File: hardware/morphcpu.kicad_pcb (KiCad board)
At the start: 2 copper layers, 70 x 70 mm, 83 parts, among them J1 TYPE-C-31-M-12, SW1 RESET, U1 ICE40UP5K-SG48I, U2 FT231XS-R, U3 W25Q32JVSSIQ, U4 ME6211C33M5G-N, U5 ME6211C12M5G-N, X1 1532H4-16000JWPDTSNL

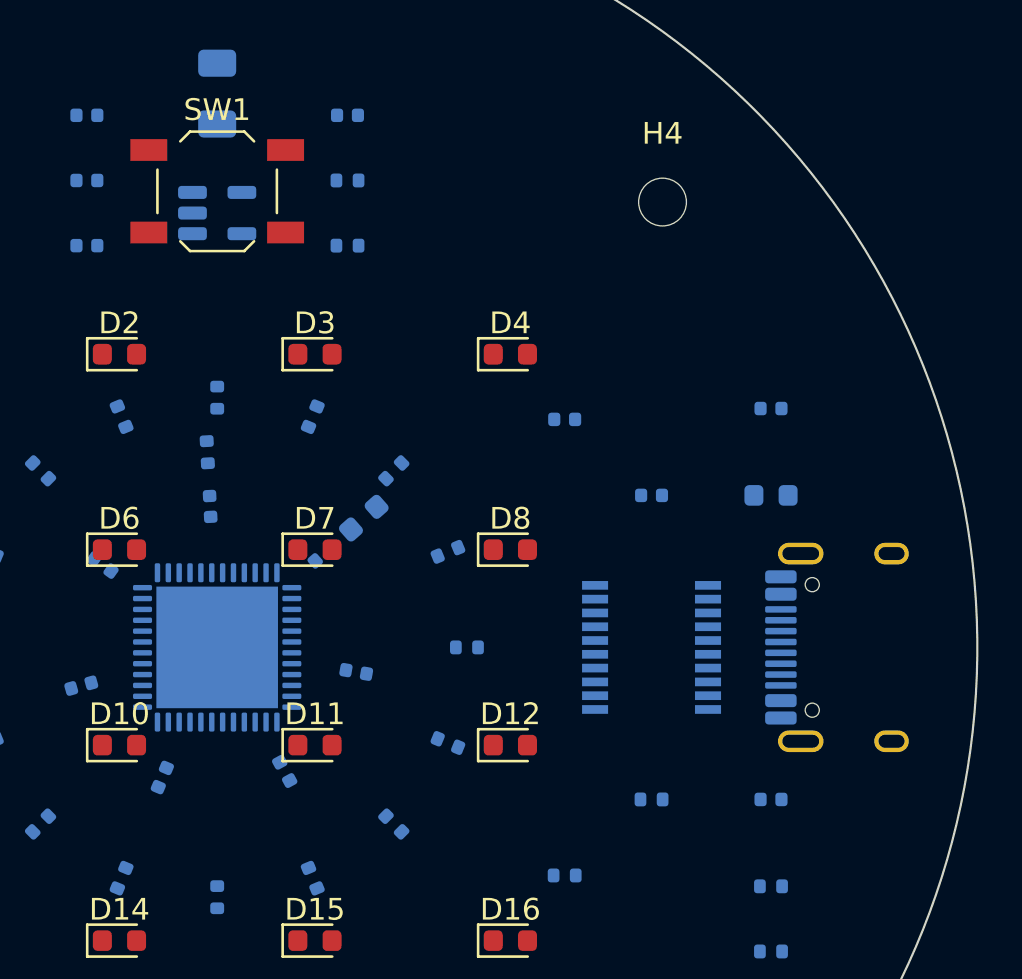
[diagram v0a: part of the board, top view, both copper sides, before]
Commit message: esd array
fixes every discrepancy between docs/BOM.md and the netlist, then pins an LCSC
part number to all 22 BOM rows so a full PCBA quote is possible.

ESD protection. BOM.md and the power tree in DESIGN.md both listed an ESD array
from the start, the schematic never had one. U6 is a USBLC6-2SC6 (C7519,
SOT-23-6) wired into the D+/D- path between J1 and U2. each protected line gets
its own net name either side of the part, USB_DP/USB_DP_F and USB_DM/USB_DM_F,
so the trace routes thru the clamp rather than stubbing off it. placed beside
the connector on the back, the U2-J1 centre line is a 1.2 mm gap, too narrow
for SOT-23-6, and the front is the LED display.

reset switch. the schematic used KiCad's SW_SPST_TL3342 land pattern (6.3 x
3.8 mm pads) but no part was pinned. the switch JLC stocks as Basic is the XKB
TS-1187A at 6.0 x 3.75 mm, close enough to pass a visual check and not close
enough to solder, so the footprint follows the part now.

counts. D17 carried the value "CDONE" and so split into its own BOM row, its
the same KT-0603R as the grid and the value field says so now, giving one LED
row of 17. BOM.md's passive counts were wrong in three places and the schematic
was right every time: 100 nF is 12 not 11, 10k is 9 not 5, and the 1k CDONE
series resistor was missing entirely.

part pinning. all 22 rows carry an LCSC number now, priced at the LCSC
lowest-quantity break. nine of the ten passive values are JLC Basic parts,
confirmed against JLC's category listings. 270R 0402 has no Basic option at JLC
at any tolerance, the alternatives were 300R/330R (changes LED current from
5 mA) or 0603 (changes 16 footprints), neither worth one feeder fee, so it
stays Extended. C7519 and C136491 are listed Extended by inference not by
quote, JLC renders its tier badge in JavaScript and neither part shows up in
the Basic listings. both need confirming in the quote.

component total is $88.06 for 5 boards now, $17.61 per board, every row re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
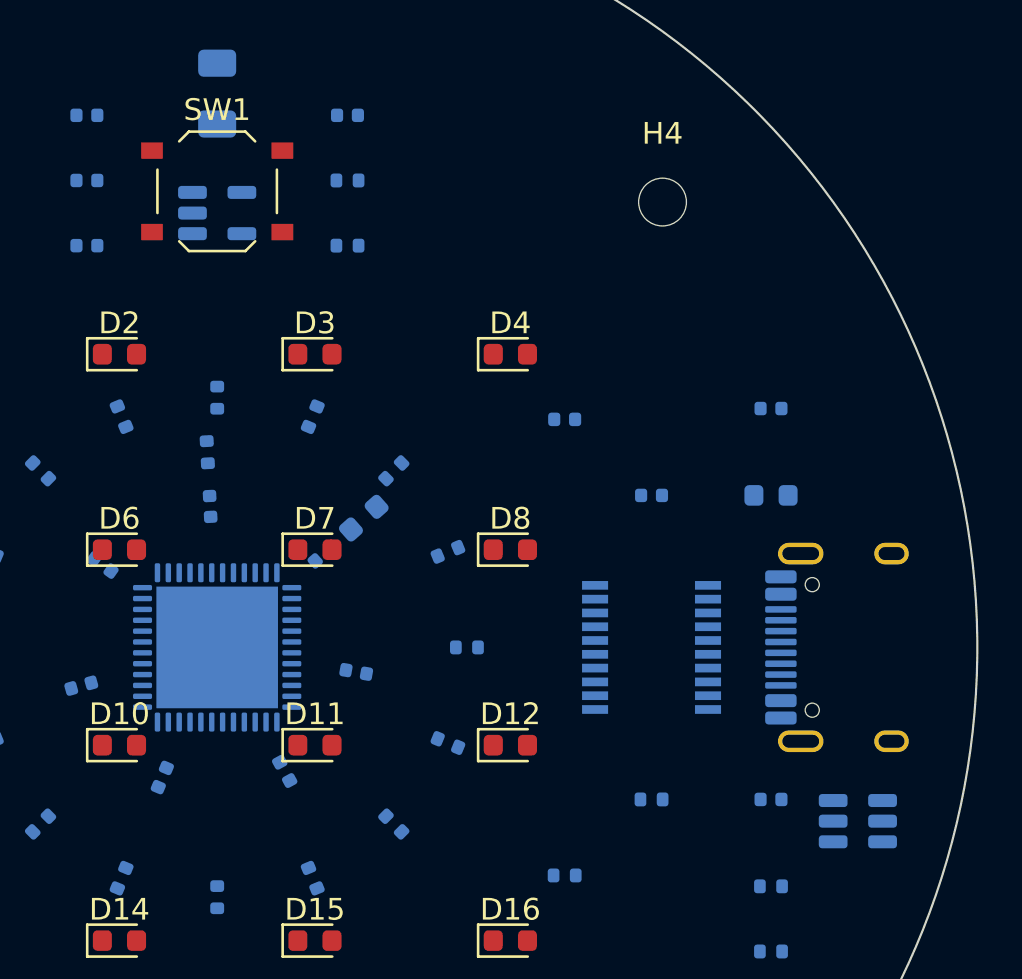
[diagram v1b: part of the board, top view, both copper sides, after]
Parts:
- added U6: USBLC6-2SC6, SOT-23-6, B.Cu at (179.5, 108.0)
- D17: value CDONE -> KT-0603R
- SW1: value RESET -> TS-1187A-B-A-B; footprint SW_SPST_TL3342 -> SW_Push_1P1T_XKB_TS-1187A
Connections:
- U2 pad 11: USB_DP -> USB_DP_F
- U2 pad 12: USB_DM -> USB_DM_F

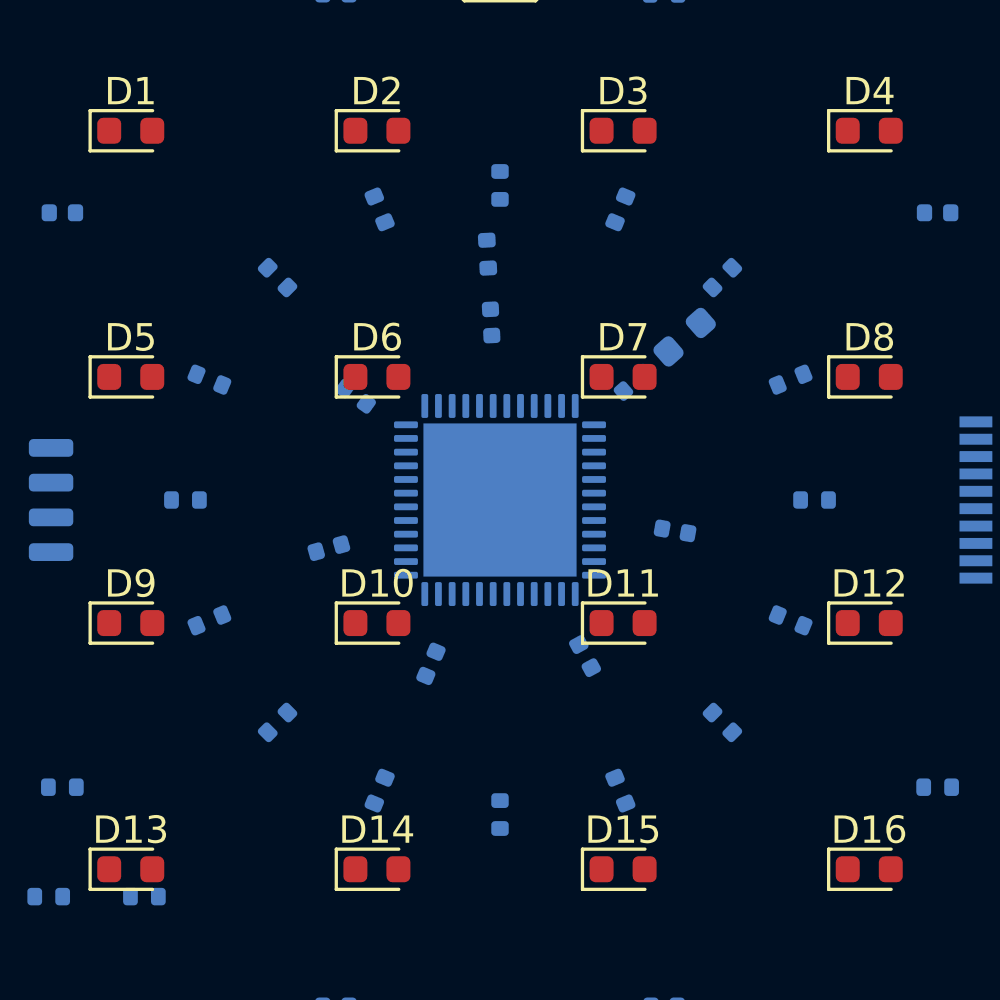
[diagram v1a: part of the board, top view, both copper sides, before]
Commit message: resistor ring pairing
still 0 tracks and 0 zones. both fixes are in the generators, not hand edits.

LED anode ratsnest 405.0 mm -> 53.4 mm.

  total anode ratsnest        405.0 mm  ->  53.4 mm
  longest single anode    31.7 (LED15_A) ->  5.21 (LED5_A, LED9_A)
  shortest                     17.7 mm  ->  1.49 mm
  chords within 5mm of centre       16  ->  0
  closest approach to centre   0.13 mm  ->  5.83 mm

gen_pcb.py sorted the LEDs by angle correctly then handed out ring slots at
k*22.5 starting from zero. the sorted list starts at -161.6 deg, so every
resistor landed 157-180 deg from its own LED and all 16 anodes ran as chords
under the QFN paddle. the sort was never the problem, the handout was.

a rotation wouldnt have fixed it either. a 4x4 grid on 9mm pitch puts the four
inner LEDs and the four corner LEDs on the same four diagonals, so eight parts
want four rays. each resistor now sits on its own LEDs ray, twelve at r=11.5
and the four corner ones at r=14.5 to break the tie. closest pair is 3.00 mm.

LED grid did NOT move. all 16 still at exact 9mm pitch, cell 0 top-left
row-major, front layer, D(n+1) still carrying LED(n)_A. verified pad by pad.

DRC after: 1 violation, a cosmetic C20/R27 silk overlap, plus the expected 167
unconnected. was 3 violations before. zero courtyard overlaps, zero shorting
pads, zero clearance errors, nothing new anywhere near the paddle.

UART off pins 6/9 onto 34/36. UART_TX_O 20.95 -> 13.99 mm, UART_RX_I
26.17 -> 19.16 mm, and neither crosses the board any more. bank 0 is the same
+3V3 VCCIO, no GBIN pin spent, no LED pin touched, no LED bank balance change.
ERC 0 errors 0 warnings.

not zero tradeoffs though: pin 35 (CLK) had empty pads either side and now sits
between two UART nets, so CLK needs a via to the front to turn west instead of
an open channel. written up in ROUTING.md, its one via over a ground pour.

34 is TX and 36 is RX, flipped vs the literal 6->34 9->36 reading. U2 pad 4 is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
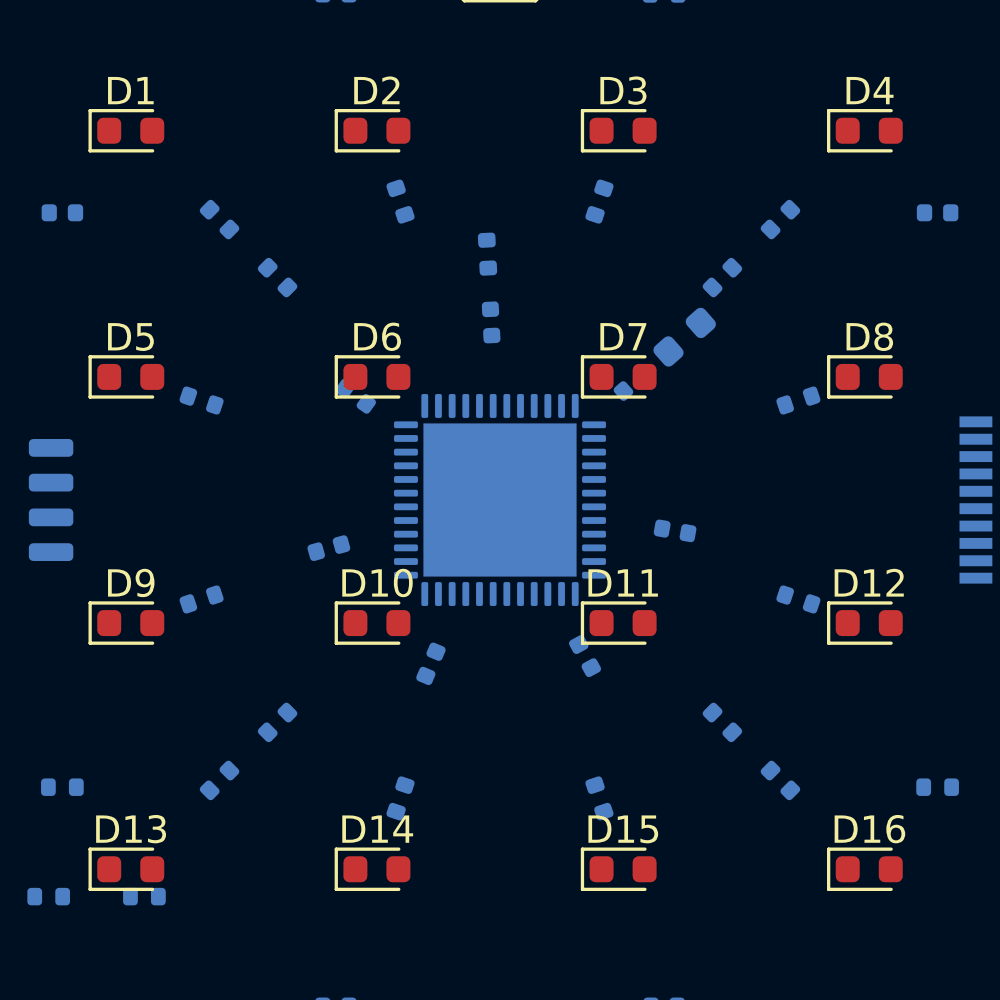
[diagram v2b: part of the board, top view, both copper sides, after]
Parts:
- moved R13 26.0 mm to (139.7, 110.3), turned to -135 degrees
- moved R16 26.0 mm to (160.3, 110.3), turned to -45 degrees
- moved R1 25.5 mm to (139.7, 89.7), turned to 135 degrees
- moved R4 25.5 mm to (160.3, 89.7), turned to 45 degrees
- moved R6 23.0 mm to (141.9, 91.9)
- moved R7 23.0 mm to (158.1, 91.9)
- moved R9 23.0 mm to (139.1, 103.6), turned to -161.565 degrees
- moved R15 23.0 mm to (153.6, 110.9), turned to -71.5651 degrees
- moved R2 23.0 mm to (146.4, 89.1), turned to 108.435 degrees
- moved R8 23.0 mm to (160.9, 96.4), turned to 18.4349 degrees
- moved R5 22.7 mm to (139.1, 96.4), turned to 161.565 degrees
- moved R3 22.7 mm to (153.6, 89.1), turned to 71.5651 degrees
- moved R14 22.7 mm to (146.4, 110.9), turned to -108.435 degrees
- moved R12 22.7 mm to (160.9, 103.6), turned to -18.4349 degrees
- moved R10 22.6 mm to (141.9, 108.1), turned to 45 degrees
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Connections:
- U1 pad 34: unconnected-(U1A-IOT_44b-Pad34) -> UART_TX_O
- U1 pad 36: unconnected-(U1A-IOT_48b-Pad36) -> UART_RX_I
- U1 pad 6: UART_RX_I -> unconnected-(U1B-IOB_13b-Pad6)
- U1 pad 9: UART_TX_O -> unconnected-(U1B-IOB_16a-Pad9)

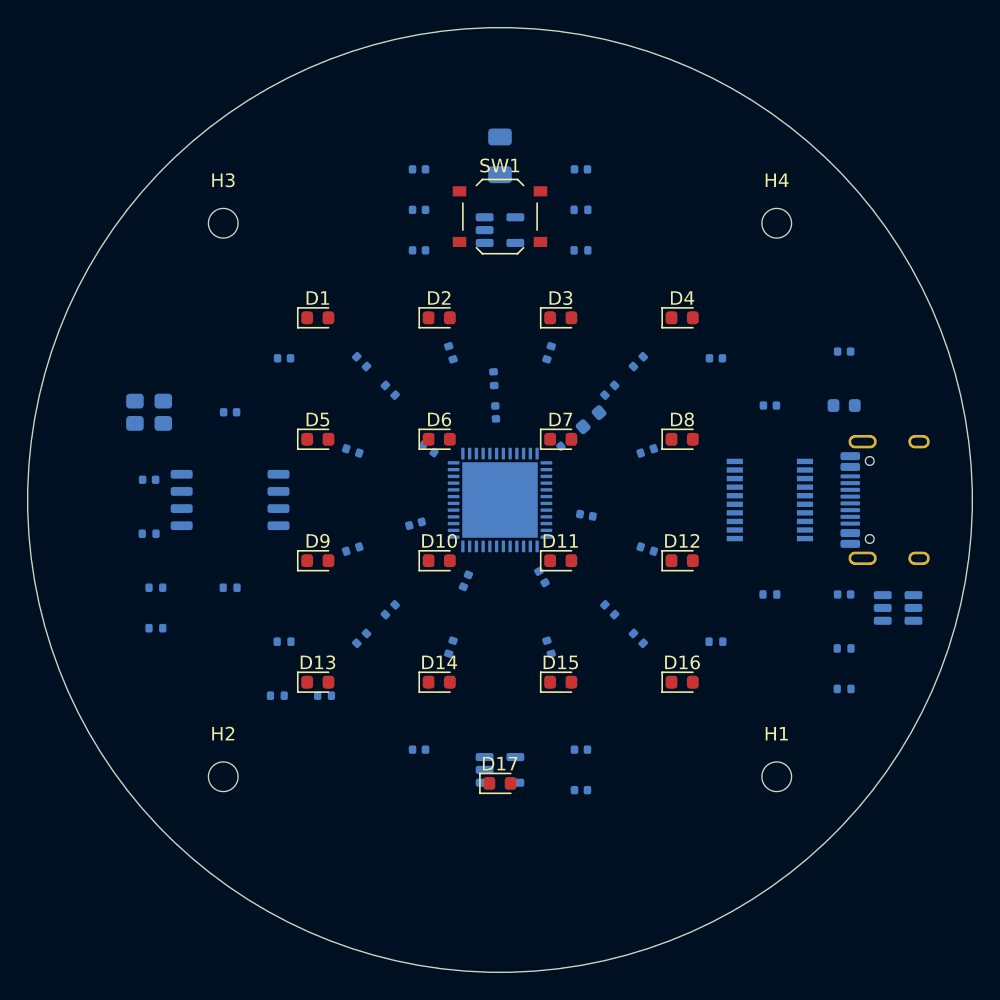
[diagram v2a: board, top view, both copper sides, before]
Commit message: freerouting attempt
reporting the real state, no cleanup applied. 865 track objects imported.

Java 25 (Temurin 25.0.4.1 LTS) unpacked to C:\Users\ranve\tools, freerouting
2.3.0 jar alongside it. winget install of Temurin 21 failed (MSI needs
elevation, UAC cancelled, exit 1602) and 21 was the wrong version anyway,
freerouting 2.3.0 is class file 69 so it needs Java 25. unpacked the Adoptium
zip instead, no admin needed, nothing added to PATH.

router ran 32 passes in 8m10s then stalled, best score 877.18 unchanged since
pass #22. optimizer gave up after one pass at 0.0000% improvement.

DRC:
  track_width        8   0.150 mm tracks against the 0.1524 mm minimum
  annular_width      2   two VBUS vias at 0.10 mm ring vs 0.15 min
  via_dangling       2   +3V3 and LED1 vias connected on one layer only
  silk_overlap       1   pre-existing C20/R27
  unconnected        8   +3V3 x3, VBUS x2, GND, LED1, +1V2, VBUS_IN

the 8 unconnected are NOT the expected GND-pour ones. GND pads are connected
because freerouting routed GND as copper anyway. -inc GND did not exclude it,
339.1 mm across 168 segments. so the pour plan is not what this board reflects.

geometry:
  F.Cu   211 segments   791.9 mm   45.9%
  B.Cu   542 segments   932.9 mm   54.1%
  total  753 segments  1724.8 mm
  vias   112  (93 at 0.6/0.3, 17 at 0.8/0.4, 2 at 0.6/0.4)

widths came back off-class in places: 8 segments at 0.1500, 16 at 0.1874, 6 at
0.2250, 5 at 0.2502, 6 at 0.3750, 3 at 0.3998. the 0.15 ones are the track_width
errors.

QFN paddle has zero vias in it. U1-49 is one of the unconnected. DESIGN.md wants
a 3x3 or 4x4 field there and it is the only ground path to the die.

front face is not clean. 211 segments and long diagonals run straight through
the LED grid. renders in docs/img/routed-3d-top.png, routed-3d-bottom.png and
the 2D copper plots for review.

no GND pour, no footprint moved, no violation fixed.
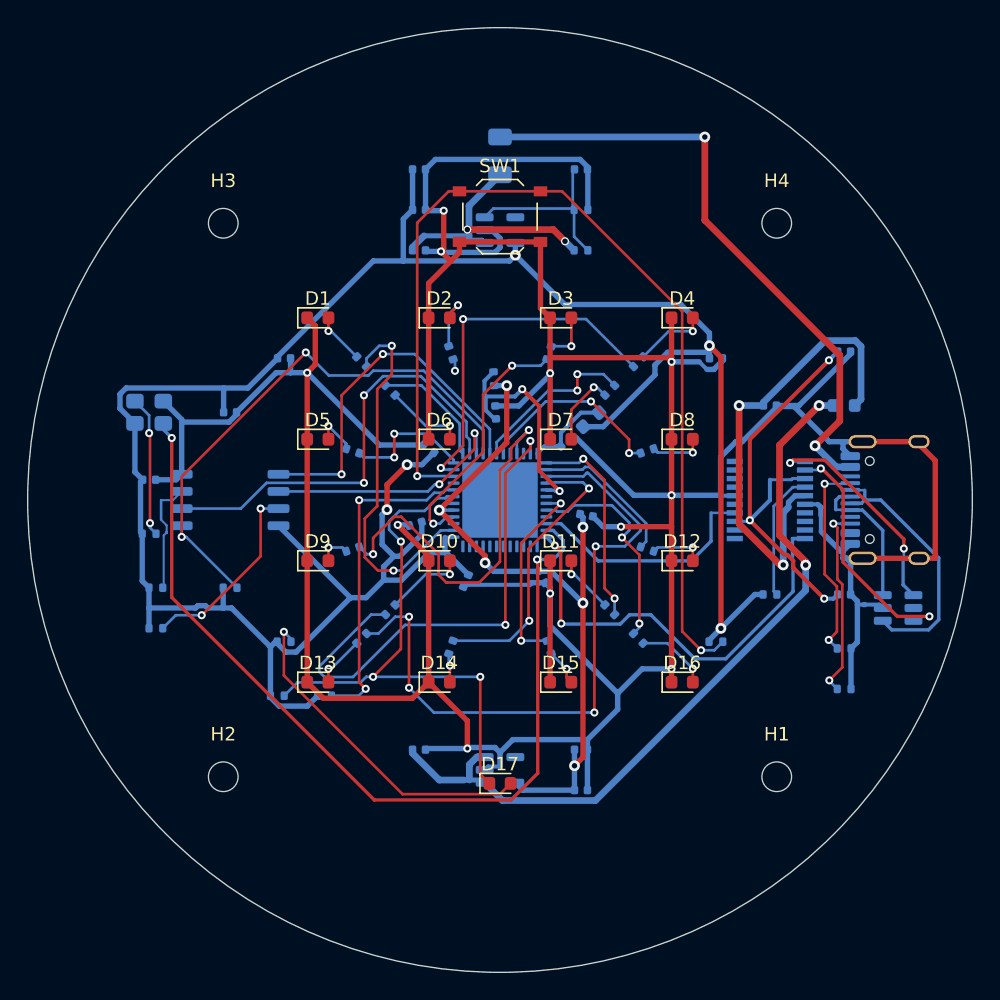
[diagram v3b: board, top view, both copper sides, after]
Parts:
- turned C2 to -61.429 degrees
- turned C4 to -164.286 degrees
- turned C21 to 41.429 degrees
- turned R8 to 18.435 degrees
- turned R14 to -108.435 degrees
- turned R12 to -18.435 degrees
- turned R15 to -71.565 degrees
- turned R2 to 108.435 degrees
- turned R5 to 161.565 degrees
- turned R3 to 71.565 degrees
- turned R9 to -161.565 degrees
- turned C5 to 144.286 degrees
- turned C3 to -112.857 degrees
- turned C20 to 92.857 degrees
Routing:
- net GND: track 0.00 -> 339.1 mm, vias 0 -> 11
- net +3V3: track 0.00 -> 183.2 mm, vias 0 -> 5
- net VBUS: track 0.00 -> 77.1 mm, vias 0 -> 4
- net RST_N: track 0.00 -> 73.3 mm, vias 0 -> 2
- net CLK: track 0.00 -> 67.6 mm, vias 0 -> 2
- net +1V2: track 0.00 -> 53.7 mm, vias 0 -> 6
- net LED12: track 0.00 -> 48.7 mm, vias 0 -> 4
- net VBUS_IN: track 0.00 -> 46.2 mm, vias 0 -> 2
- net CDONE: track 0.00 -> 41.6 mm, vias 0 -> 3
- net FLASH_CS: track 0.00 -> 41.5 mm, vias 0 -> 2
- net LED9: track 0.00 -> 37.8 mm, vias 0 -> 2
- net FT_VCC: track 0.00 -> 35.5 mm, vias 0 -> 2
- net UART_RX_I: track 0.00 -> 33.5 mm, vias 0 -> 2
- net FLASH_DO: track 0.00 -> 32.8 mm, vias 0 -> 2
- net FT_3V3: track 0.00 -> 32.0 mm, vias 0 -> 3
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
